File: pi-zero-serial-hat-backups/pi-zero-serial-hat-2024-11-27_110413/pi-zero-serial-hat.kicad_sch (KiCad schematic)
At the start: 56 parts, among them J1 Conn_02x20_Counter_Clockwise, J2 Screw_Terminal_01x03, J3 Conn_01x02_Pin, J4 Conn_01x02_Pin, J5 Screw_Terminal_01x02, Q1 AOD4184, Q2 AOD4184, U1 MAX13487EESAT, U2 CX8571

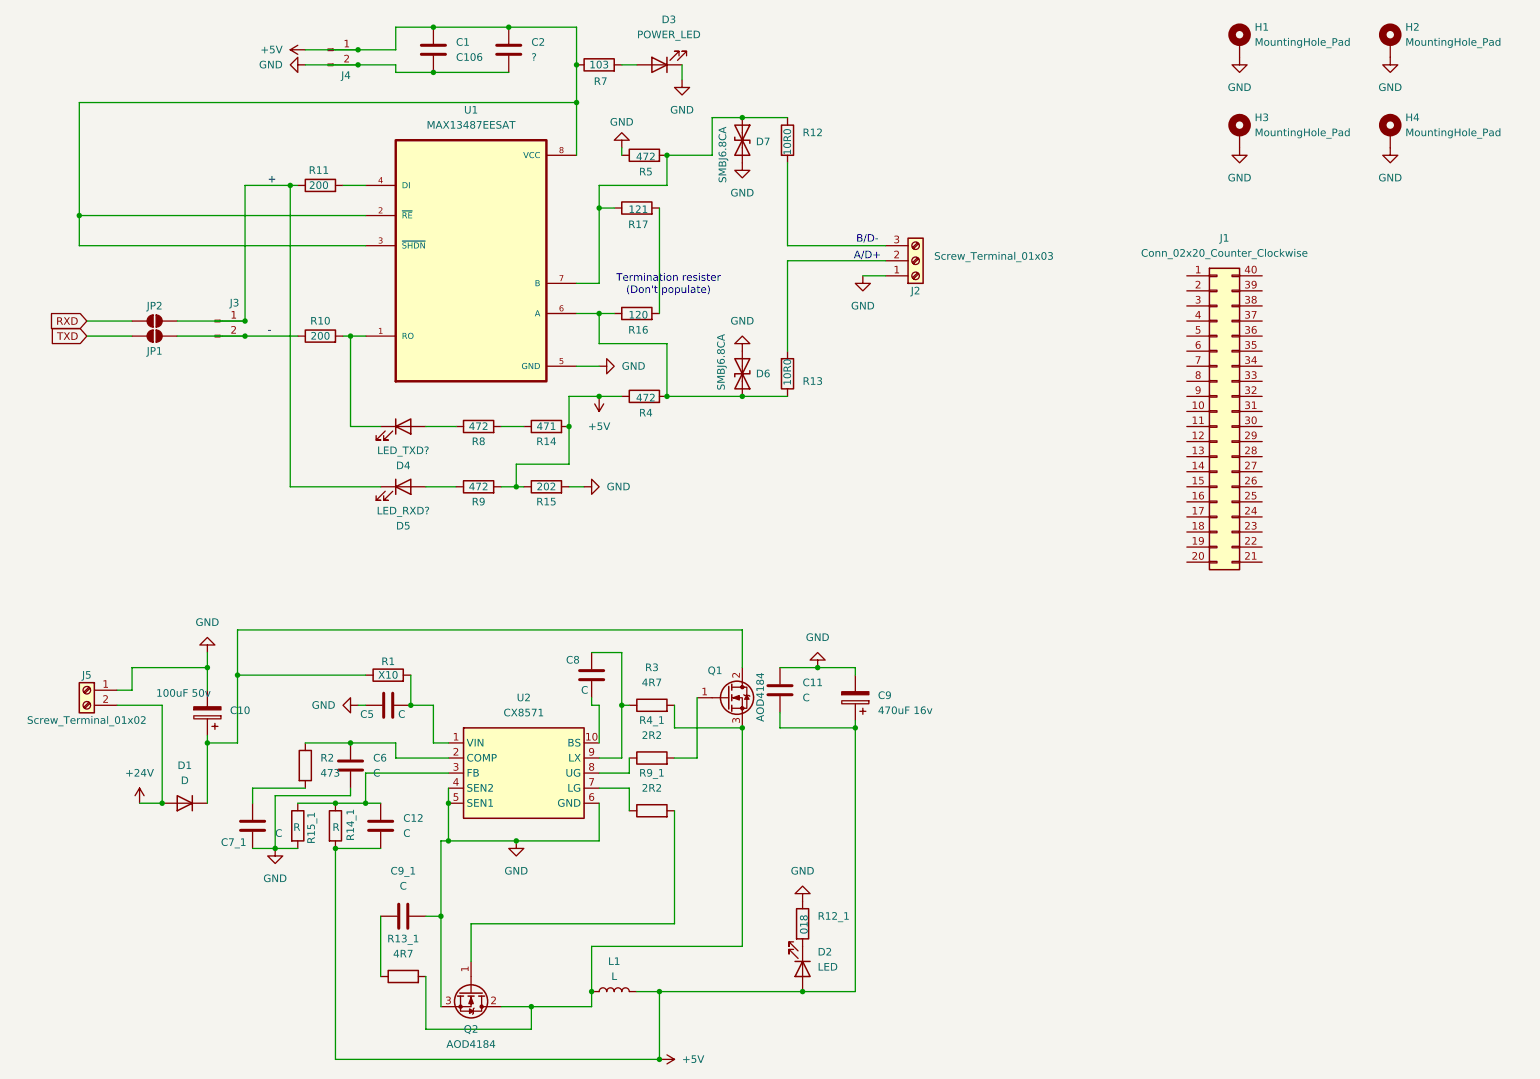
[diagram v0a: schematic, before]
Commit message: Added schematic from reversed board
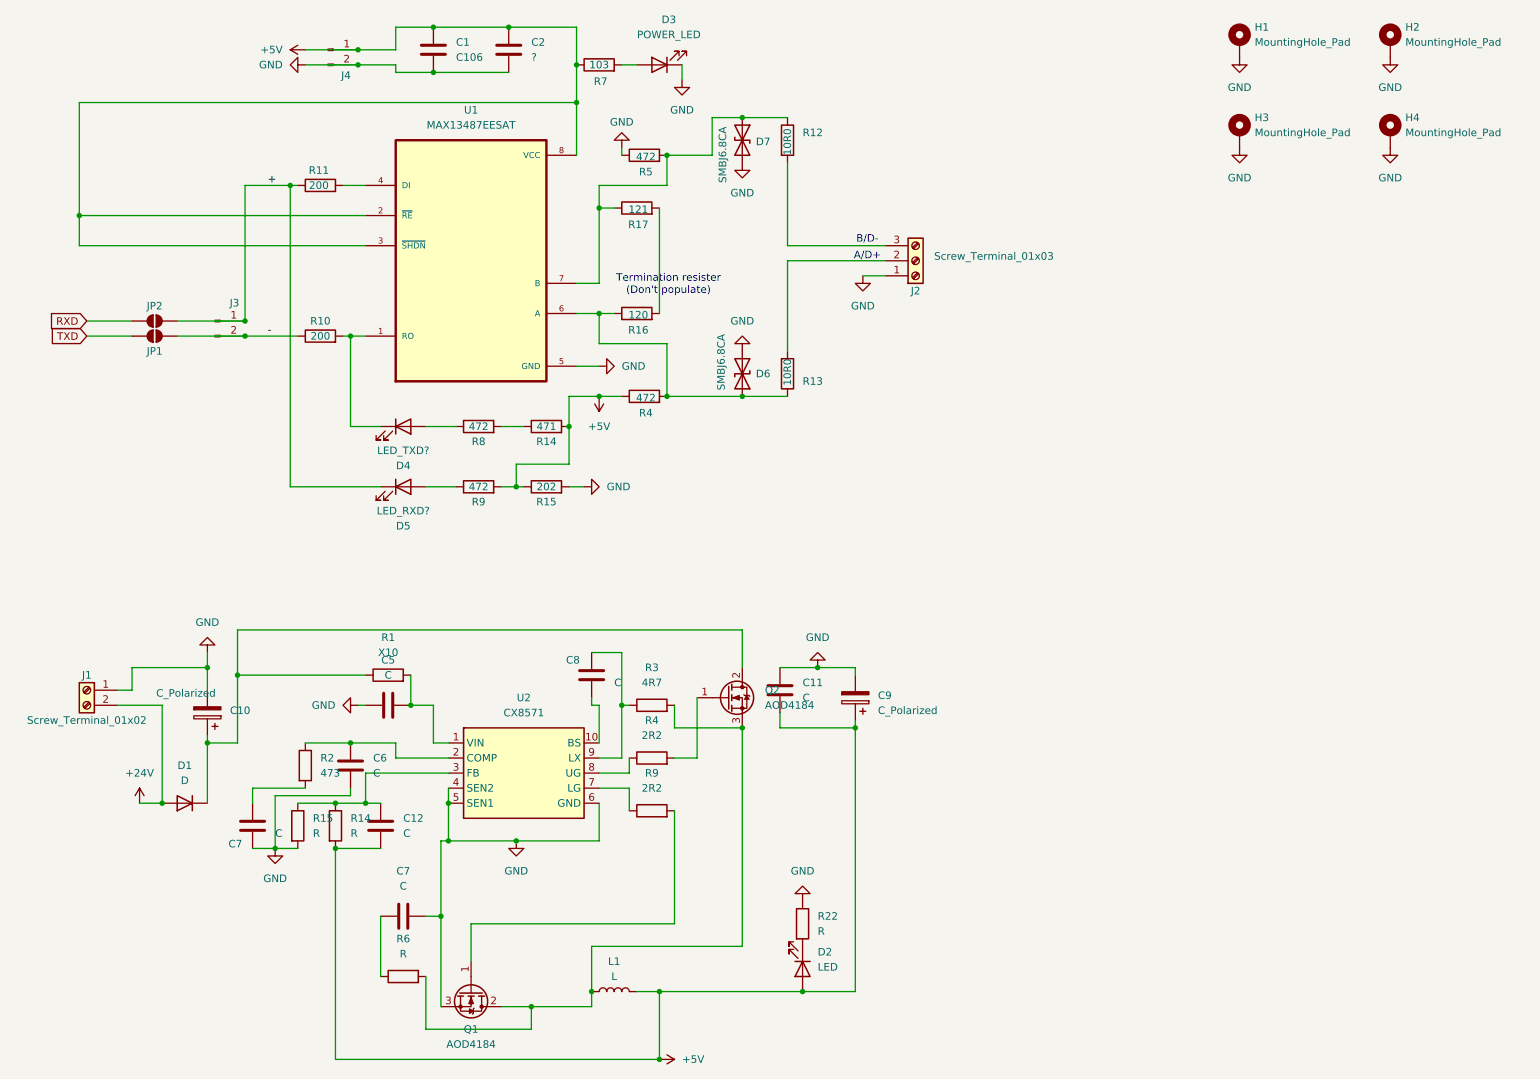
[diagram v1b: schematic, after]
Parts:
- removed J1: Conn_02x20_Counter_Clockwise, lib:PinSocket_2x20_P2.54mm_Vertical_Centered_Anchor, symbol Connector_Generic:Conn_02x20_Counter_Clockwise
- C10: value 100uF 50v -> C_Polarized
- C9: value 470uF 16v -> C_Polarized
- J1: renamed from J5; footprint TerminalBlock_RND:TerminalBlock_RND_205-00012_1x02_P5.00mm_Horizontal -> TerminalBlock_RND:TerminalBlock_RND_205-00013_1x02_P5.00mm_Horizontal
- R22: renamed from R12_1; value 018 -> R
- R6: renamed from R13_1; value 4R7 -> R
- renumbered C7_1 to C7, C9_1 to C7, Q2 to Q1, Q1 to Q2, R14_1 to R14, R15_1 to R15, R4_1 to R4, R9_1 to R9
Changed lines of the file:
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@@
 		)
 		(property "Value" "C"
-			(at 107.442 129.54 0)
+			(at 113.03 128.2699 0)
 			(effects
 				(font
@@
 		(dnp no)
 		(fields_autoplaced yes)
-		(property "Reference" "R9_1"
+		(property "Reference" "R9"
 			(at 119.38 143.51 90)
 			(effects
@@
 			(project "pi-zero-serial-hat"
 				(path "/86197b65-cdb8-4141-8c86-0c94c717a4aa"
-					(reference "R9_1")
+					(reference "R9")
 					(unit 1)
 				)
@@
 		(on_board yes)
 		(dnp no)
-		(property "Reference" "C7_1"
-			(at 46.736 155.194 0)
+		(property "Reference" "C7"
+			(at 48.006 155.448 0)
 			(effects
 				(font
@@
 			(project ""
 				(path "/86197b65-cdb8-4141-8c86-0c94c717a4aa"
-					(reference "C7_1")
+					(reference "C7")
 					(unit 1)
 				)
@@
 		(on_board yes)
 		(dnp no)
-		(property "Reference" "R14_1"
-			(at 68.58 154.94 90)
+		(fields_autoplaced yes)
+		(property "Reference" "R14"
+			(at 68.58 151.1299 0)
 			(effects
 				(font
@@
 		)
 		(property "Value" "R"
-			(at 65.532 152.654 0)
+			(at 68.58 153.6699 0)
 			(effects
 				(font
@@
 			(project "pi-zero-serial-hat"
 				(path "/86197b65-cdb8-4141-8c86-0c94c717a4aa"
-					(reference "R14_1")
+					(reference "R14")
 					(unit 1)
 				)
@@
 		(on_board yes)
 		(dnp no)
-		(property "Reference" "R12_1"
+		(fields_autoplaced yes)
+		(property "Reference" "R22"
 			(at 147.32 167.6399 0)
 			(effects
@@
 			)
 		)
-		(property "Value" "018"
-			(at 145.034 170.688 90)
+		(property "Value" "R"
+			(at 147.32 170.1799 0)
 			(effects
 				(font
@@
 			(project "pi-zero-serial-hat"
 				(path "/86197b65-cdb8-4141-8c86-0c94c717a4aa"
-					(reference "R12_1")
+					(reference "R22")
 					(unit 1)
 				)
@@
 		(dnp no)
 		(fields_autoplaced yes)
-		(property "Reference" "R4_1"
+		(property "Reference" "R4"
 			(at 119.38 134.62 90)
 			(effects
@@
 			(project "pi-zero-serial-hat"
 				(path "/86197b65-cdb8-4141-8c86-0c94c717a4aa"
-					(reference "R4_1")
+					(reference "R4")
 					(unit 1)
 				)
@@
 		(dnp no)
 		(fields_autoplaced yes)
-		(property "Reference" "R13_1"
+		(property "Reference" "R6"
 			(at 77.47 171.45 90)
 			(effects
@@
 			)
 		)
-		(property "Value" "4R7"
+		(property "Value" "R"
 			(at 77.47 173.99 90)
 			(effects
@@
 			(project "pi-zero-serial-hat"
 				(path "/86197b65-cdb8-4141-8c86-0c94c717a4aa"
-					(reference "R13_1")
+					(reference "R6")
 					(unit 1)
 				)
@@
 		(on_board yes)
 		(dnp no)
-		(property "Reference" "R15_1"
-			(at 61.976 155.448 90)
+		(fields_autoplaced yes)
+		(property "Reference" "R15"
+			(at 62.23 151.1299 0)
 			(effects
 				(font
@@
 		)
 		(property "Value" "R"
-			(at 58.928 152.654 0)
+			(at 62.23 153.6699 0)
 			(effects
 				(font
@@
 			(project ""
 				(path "/86197b65-cdb8-4141-8c86-0c94c717a4aa"
-					(reference "R15_1")
+					(reference "R15")
 					(unit 1)
 				)
@@
 		(on_board yes)
 		(dnp no)
+		(fields_autoplaced yes)
 		(property "Reference" "R1"
-			(at 74.93 124.714 90)
+			(at 74.93 120.65 90)
 			(effects
 				(font
@@
 		)
 		(property "Value" "X10"
-			(at 74.93 127 90)
+			(at 74.93 123.19 90)
 			(effects
 				(font
@@
 		(dnp no)
 		(fields_autoplaced yes)
-		(property "Reference" "C9_1"
+		(property "Reference" "C7"
 			(at 77.47 160.02 90)
 			(effects
@@
 			(project "pi-zero-serial-hat"
 				(path "/86197b65-cdb8-4141-8c86-0c94c717a4aa"
-					(reference "C9_1")
+					(reference "C7")
 					(unit 1)
 				)
@@
 			)
 		)
-		(property "Value" "100uF 50v"
+		(property "Value" "C_Polarized"
 			(at 35.814 130.048 0)
 			(effects
@@
 			)
 		)
-		(property "Value" "470uF 16v"
+		(property "Value" "C_Polarized"
 			(at 157.48 132.9689 0)
 			(effects
@@
 		(on_board yes)
 		(dnp no)
+		(fields_autoplaced yes)
 		(property "Reference" "C5"
-			(at 71.374 133.604 90)
+			(at 74.93 124.46 90)
 			(effects
 				(font
@@
 		)
 		(property "Value" "C"
-			(at 77.216 133.604 90)
+			(at 74.93 127 90)
 			(effects
 				(font
@@
 	)
 	(symbol
-		(lib_id "Connector_Generic:Conn_02x20_Counter_Clockwise")
-		(at 214.63 82.55 0)
-		(unit 1)
-		(exclude_from_sim no)
-		(in_bom yes)
-		(on_board yes)
-		(dnp no)
-		(fields_autoplaced yes)
-		(property "Reference" "J1"
-			(at 215.9 53.34 0)
-			(effects
-				(font
-					(size 1.27 1.27)
-				)
-			)
-		)
-		(property "Value" "Conn_02x20_Counter_Clockwise"
-			(at 215.9 55.88 0)
-			(effects
-				(font
-					(size 1.27 1.27)
-				)
-			)
-		)
-		(property "Footprint" "lib:PinSocket_2x20_P2.54mm_Vertical_Centered_Anchor"
-			(at 214.63 82.55 0)
-			(effects
-				(font
-					(size 1.27 1.27)
-				)
-				(hide yes)
-			)
-		)
-		(property "Datasheet" "~"
-			(at 214.63 82.55 0)
-			(effects
-				(font
-					(size 1.27 1.27)
-				)
-				(hide yes)
-			)
-		)
-		(property "Description" "Generic connector, double row, 02x20, counter clockwise pin numbering scheme (similar to DIP package numbering), script generated (kicad-library-utils/schlib/autogen/connector/)"
-			(at 214.63 82.55 0)
-			(effects
-				(font
-					(size 1.27 1.27)
-				)
-				(hide yes)
-			)
-		)
-		(pin "26"
-		)
-		(pin "16"
-		)
-		(pin "14"
-		)
-		(pin "17"
-		)
-		(pin "25"
-		)
-		(pin "15"
-		)
-		(pin "18"
-		)
-		(pin "19"
-		)
-		(pin "28"
-		)
-		(pin "13"
-		)
-		(pin "11"
-		)
-		(pin "10"
-		)
-		(pin "2"
-		)
-		(pin "9"
-		)
-		(pin "1"
-		)
-		(pin "12"
-		)
-		(pin "34"
-		)
-		(pin "7"
-		)
-		(pin "27"
-		)
-		(pin "22"
-		)
-		(pin "3"
-		)
-		(pin "38"
-		)
-		(pin "31"
-		)
-		(pin "6"
-		)
-		(pin "39"
-		)
-		(pin "33"
-		)
-		(pin "32"
-		)
-		(pin "5"
-		)
-		(pin "8"
-		)
-		(pin "40"
-		)
-		(pin "23"
-		)
-		(pin "20"
-		)
-		(pin "36"
-		)
-		(pin "21"
-		)
-		(pin "37"
-		)
-		(pin "35"
-		)
-		(pin "29"
-		)
-		(pin "24"
-		)
-		(pin "30"
-		)
-		(pin "4"
-		)
-		(instances
-			(project ""
-				(path "/86197b65-cdb8-4141-8c86-0c94c717a4aa"
-					(reference "J1")
-					(unit 1)
-				)
-			)
-		)
-	)
-	(symbol
 		(lib_id "Connector:Screw_Terminal_01x02")
 		(at 24.13 129.54 0)
@@
 		(on_board yes)
 		(dnp no)
-		(property "Reference" "J5"
+		(property "Reference" "J1"
 			(at 24.13 127 0)
 			(effects
@@
 			)
 		)
-		(property "Footprint" "TerminalBlock_RND:TerminalBlock_RND_205-00012_1x02_P5.00mm_Horizontal"
+		(property "Footprint" "TerminalBlock_RND:TerminalBlock_RND_205-00013_1x02_P5.00mm_Horizontal"
 			(at 24.13 129.54 0)
 			(effects
@@
 			(project "pi-zero-serial-hat"
 				(path "/86197b65-cdb8-4141-8c86-0c94c717a4aa"
-					(reference "J5")
+					(reference "J1")
 					(unit 1)
 				)
@@
 		(on_board yes)
 		(dnp no)
-		(property "Reference" "Q1"
-			(at 128.778 126.238 0)
+		(fields_autoplaced yes)
+		(property "Reference" "Q2"
+			(at 138.43 129.5399 0)
 			(effects
 				(font
@@
 		)
 		(property "Value" "AOD4184"
-			(at 137.668 134.874 90)
+			(at 138.43 132.0799 0)
 			(effects
 				(font
@@
 			(project "pi-zero-serial-hat"
 				(path "/86197b65-cdb8-4141-8c86-0c94c717a4aa"
-					(reference "Q1")
+					(reference "Q2")
 					(unit 1)
 				)
@@
 		(dnp no)
 		(fields_autoplaced yes)
-		(property "Reference" "Q2"
+		(property "Reference" "Q1"
 			(at 88.9 186.69 90)
 			(effects
@@
 			(project ""
 				(path "/86197b65-cdb8-4141-8c86-0c94c717a4aa"
-					(reference "Q2")
+					(reference "Q1")
 					(unit 1)
 				)
